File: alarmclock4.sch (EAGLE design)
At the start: 33 parts, among them X1 MKDSN1,5/2-5,08, X2 MKDSN1,5/2-5,08, X3 MKDSN1,5/2-5,08, X4 MKDSN1,5/2-5,08

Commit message: new board
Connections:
- net GND: now also U$1.GND1
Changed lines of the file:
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@@
 <?xml version="1.0" encoding="utf-8"?>
 <!DOCTYPE eagle SYSTEM "eagle.dtd">
-<eagle version="6.6.0">
+<eagle version="7.6.0">
 <drawing>
 <settings>
@@
 <layers>
 <layer number="1" name="Top" color="4" fill="1" visible="no" active="no"/>
+<layer number="2" name="Route2" color="1" fill="3" visible="no" active="no"/>
+<layer number="3" name="Route3" color="4" fill="3" visible="no" active="no"/>
+<layer number="14" name="Route14" color="1" fill="6" visible="no" active="no"/>
+<layer number="15" name="Route15" color="4" fill="6" visible="no" active="no"/>
 <layer number="16" name="Bottom" color="1" fill="1" visible="no" active="no"/>
 <layer number="17" name="Pads" color="2" fill="1" visible="no" active="no"/>
@@
 <pinref part="U$3" gate="G$1" pin="PVDD_D2"/>
 <wire x1="157.48" y1="17.78" x2="157.48" y2="15.24" width="0.1524" layer="91"/>
+<junction x="157.48" y="17.78"/>
 </segment>
 <segment>
@@
 <pinref part="U$3" gate="G$1" pin="PVDD_C2"/>
 <wire x1="157.48" y1="-5.08" x2="157.48" y2="-7.62" width="0.1524" layer="91"/>
+<junction x="157.48" y="-5.08"/>
 </segment>
 <segment>
@@
 <pinref part="U$3" gate="G$1" pin="PVDD_B2"/>
 <wire x1="157.48" y1="-27.94" x2="157.48" y2="-30.48" width="0.1524" layer="91"/>
+<junction x="157.48" y="-27.94"/>
 </segment>
 <segment>
@@
 <pinref part="SUPPLY2" gate="G$1" pin="VCC"/>
 <wire x1="157.48" y1="-50.8" x2="160.02" y2="-50.8" width="0.1524" layer="91"/>
+<junction x="157.48" y="-50.8"/>
 </segment>
 </net>
@@
 <wire x1="127" y1="73.66" x2="111.76" y2="73.66" width="0.1524" layer="91"/>
 <junction x="127" y="73.66"/>
+<wire x1="134.62" y1="73.66" x2="134.62" y2="68.58" width="0.1524" layer="91"/>
+<wire x1="134.62" y1="68.58" x2="154.94" y2="68.58" width="0.1524" layer="91"/>
+<pinref part="U$1" gate="G$1" pin="GND1"/>
+<wire x1="154.94" y1="68.58" x2="154.94" y2="76.2" width="0.1524" layer="91"/>
+<junction x="134.62" y="73.66"/>
 </segment>
 <segment>
@@
 <pinref part="R3" gate="G$1" pin="1"/>
 <pinref part="SUPPLY26" gate="GND" pin="GND"/>
+<junction x="134.62" y="-83.82"/>
 </segment>
 <segment>
@@
 <pinref part="C14" gate="G$1" pin="2"/>
 <pinref part="U$6" gate="G$1" pin="P$1"/>
+<junction x="172.72" y="12.7"/>
 </segment>
 </net>
@@
 <pinref part="C4" gate="G$1" pin="2"/>
 <pinref part="U$9" gate="G$1" pin="P$1"/>
+<junction x="172.72" y="-55.88"/>
 </segment>
 </net>
@@
 <pinref part="C3" gate="G$1" pin="2"/>
 <pinref part="U$8" gate="G$1" pin="P$1"/>
+<junction x="172.72" y="-33.02"/>
 </segment>
 </net>
@@
 <pinref part="C2" gate="G$1" pin="2"/>
 <pinref part="U$7" gate="G$1" pin="P$1"/>
+<junction x="172.72" y="-10.16"/>
 </segment>
 </net>
@@
 <pinref part="C6" gate="G$1" pin="1"/>
 <pinref part="U$8" gate="G$1" pin="P$2"/>
+<junction x="210.82" y="-33.02"/>
 </segment>
 </net>
@@
 <pinref part="C6" gate="G$1" pin="2"/>
 <pinref part="U$9" gate="G$1" pin="P$2"/>
+<junction x="210.82" y="-55.88"/>
 </segment>
 </net>
@@
 <pinref part="C5" gate="G$1" pin="2"/>
 <pinref part="U$7" gate="G$1" pin="P$2"/>
+<junction x="210.82" y="-10.16"/>
 </segment>
 </net>
@@
 <pinref part="C5" gate="G$1" pin="1"/>
 <pinref part="U$6" gate="G$1" pin="P$2"/>
+<junction x="210.82" y="12.7"/>
 </segment>
 </net>
@@
 <pinref part="C7" gate="G$1" pin="1"/>
 <pinref part="R5" gate="G$1" pin="2"/>
+<junction x="55.88" y="-38.1"/>
 </segment>
 </net>
@@
 <junction x="20.32" y="22.86"/>
 <wire x1="20.32" y1="22.86" x2="20.32" y2="17.78" width="0.1524" layer="91"/>
-<wire x1="20.32" y1="22.86" x2="20.32" y2="12.7" width="0.1524" layer="91"/>
+<wire x1="20.32" y1="22.86" x2="20.32" y2="17.78" width="0.1524" layer="91"/>
+<junction x="20.32" y="17.78"/>
+<wire x1="20.32" y1="17.78" x2="20.32" y2="12.7" width="0.1524" layer="91"/>
 </segment>
 </net>
@@
 <wire x1="-53.34" y1="-17.78" x2="-53.34" y2="-43.18" width="0.1524" layer="91"/>
 <wire x1="-53.34" y1="-43.18" x2="-63.5" y2="-43.18" width="0.1524" layer="91"/>
+<junction x="-63.5" y="-43.18"/>
 </segment>
 </net>
@@
 <wire x1="-53.34" y1="-12.7" x2="-53.34" y2="-7.62" width="0.1524" layer="91"/>
 <wire x1="-53.34" y1="-7.62" x2="-63.5" y2="-7.62" width="0.1524" layer="91"/>
+<junction x="-63.5" y="-7.62"/>
 </segment>
 </net>
@@
 </sheet>
 </sheets>
+<errors>
+</errors>
 </schematic>
 </drawing>

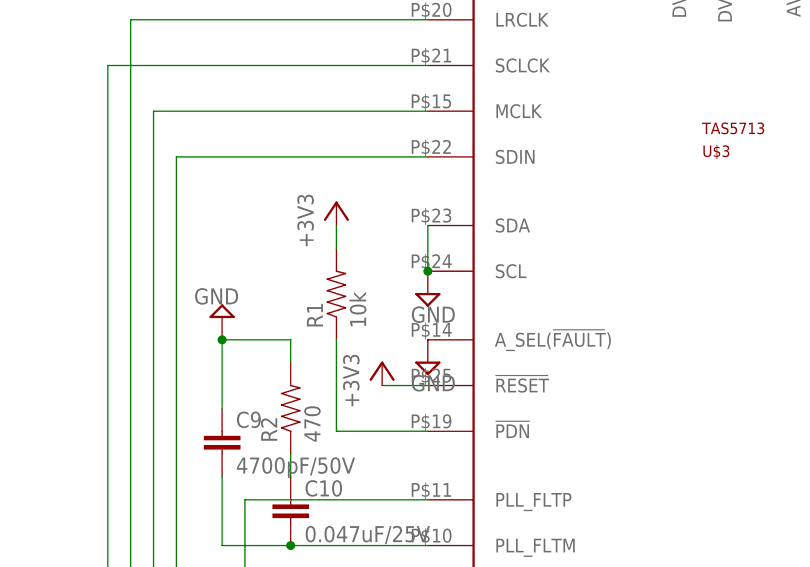
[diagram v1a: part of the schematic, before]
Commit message: - 2 bugfix: orientation of dc-dc + TAS pin SEL must not be to ground - remove via under the TAS chip
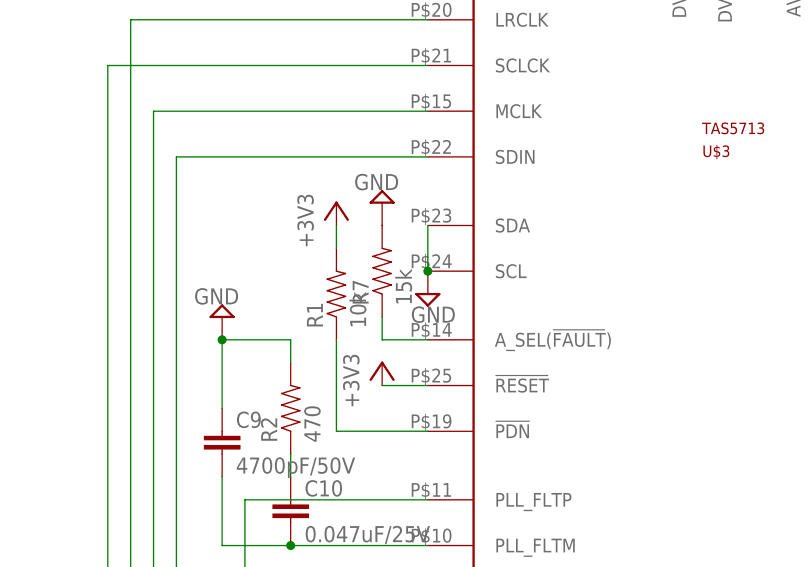
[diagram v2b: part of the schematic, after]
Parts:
- added R7: 15k, SparkFun-Passives:RESISTOR0603-RES
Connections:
- new net N$34: R7.1, U$3.A_SEL(!FAULT!)
- net GND: now also R7.2; no longer U$3.A_SEL(!FAULT!)
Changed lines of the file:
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@@
 <part name="+3V7" library="supply1" deviceset="+3V3" device=""/>
 <part name="SUPPLY29" library="supply2" deviceset="GND" device=""/>
+<part name="R7" library="SparkFun-Passives" deviceset="RESISTOR" device="0603-RES" value="15k"/>
 </parts>
 <sheets>
@@
 <instance part="SUPPLY17" gate="GND" x="20.32" y="5.08"/>
 <instance part="SUPPLY18" gate="GND" x="76.2" y="-5.08"/>
-<instance part="SUPPLY19" gate="GND" x="76.2" y="-12.7"/>
+<instance part="SUPPLY19" gate="GND" x="71.12" y="5.08" rot="R180"/>
 <instance part="SUPPLY20" gate="GND" x="76.2" y="-43.18"/>
 <instance part="SUPPLY21" gate="GND" x="76.2" y="-55.88"/>
@@
 <instance part="+3V7" gate="G$1" x="-60.96" y="53.34"/>
 <instance part="SUPPLY29" gate="GND" x="-60.96" y="22.86"/>
+<instance part="R7" gate="G$1" x="71.12" y="-2.54" rot="R90"/>
 </instances>
 <busses>
@@
 </segment>
 <segment>
-<pinref part="U$3" gate="G$1" pin="A_SEL(!FAULT!)"/>
-<pinref part="SUPPLY19" gate="GND" pin="GND"/>
-</segment>
-<segment>
 <pinref part="U$3" gate="G$1" pin="SCL"/>
 <pinref part="U$3" gate="G$1" pin="SDA"/>
@@
 <pinref part="U$10" gate="G$1" pin="GND"/>
 <pinref part="SUPPLY29" gate="GND" pin="GND"/>
+</segment>
+<segment>
+<pinref part="R7" gate="G$1" pin="2"/>
+<pinref part="SUPPLY19" gate="GND" pin="GND"/>
 </segment>
 </net>
@@
 </segment>
 </net>
+<net name="N$34" class="0">
+<segment>
+<pinref part="R7" gate="G$1" pin="1"/>
+<wire x1="71.12" y1="-7.62" x2="71.12" y2="-10.16" width="0.1524" layer="91"/>
+<pinref part="U$3" gate="G$1" pin="A_SEL(!FAULT!)"/>
+<wire x1="71.12" y1="-10.16" x2="76.2" y2="-10.16" width="0.1524" layer="91"/>
+</segment>
+</net>
